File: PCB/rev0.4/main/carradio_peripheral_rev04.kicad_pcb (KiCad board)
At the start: 4 copper layers, 100 x 100 mm, 210 parts, among them J1 ISO 10487 A (via pigtail), J10 Expansion, J12 Display buttons, J13 HDMI in (from VIM3), J14 Display FPC 40P 0.5mm, J18 VIM3 VIN (JST-XH 2P), J2 VIM3 40-pin via 2x20 IDC ribb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, J21 Expansion 2, J22 SWD, J23 Audio module socket, J25 USB module socket, J27 GNSS module socket, J5 VIM3 POWER key lead, J7 BH1750 light sensor, J8 ISO 10487 C1 (via pigtail), Q1 AO3400A, Q10 P-MOSFET -40V, Q11 CSD18543Q3A, Q12 CSD18543Q3A, Q2 P-MOSFET -60V, Q3 2N7002, SW1 BOOTSEL, SW2 RESET, U1 TPS560430XDBVR, U12 TPS55288RPMR, U13 CH334R, U19 AP2112K-3.3, U2 EL817S1(C), U20 RP2350B, U21 W25Q128JVS, U3 EL817S1(C), U4 EL817S1(C), U5 EL817S1(C), U6 LP5907MFX-3.3, Y1 12MHz, Y3 12MHz

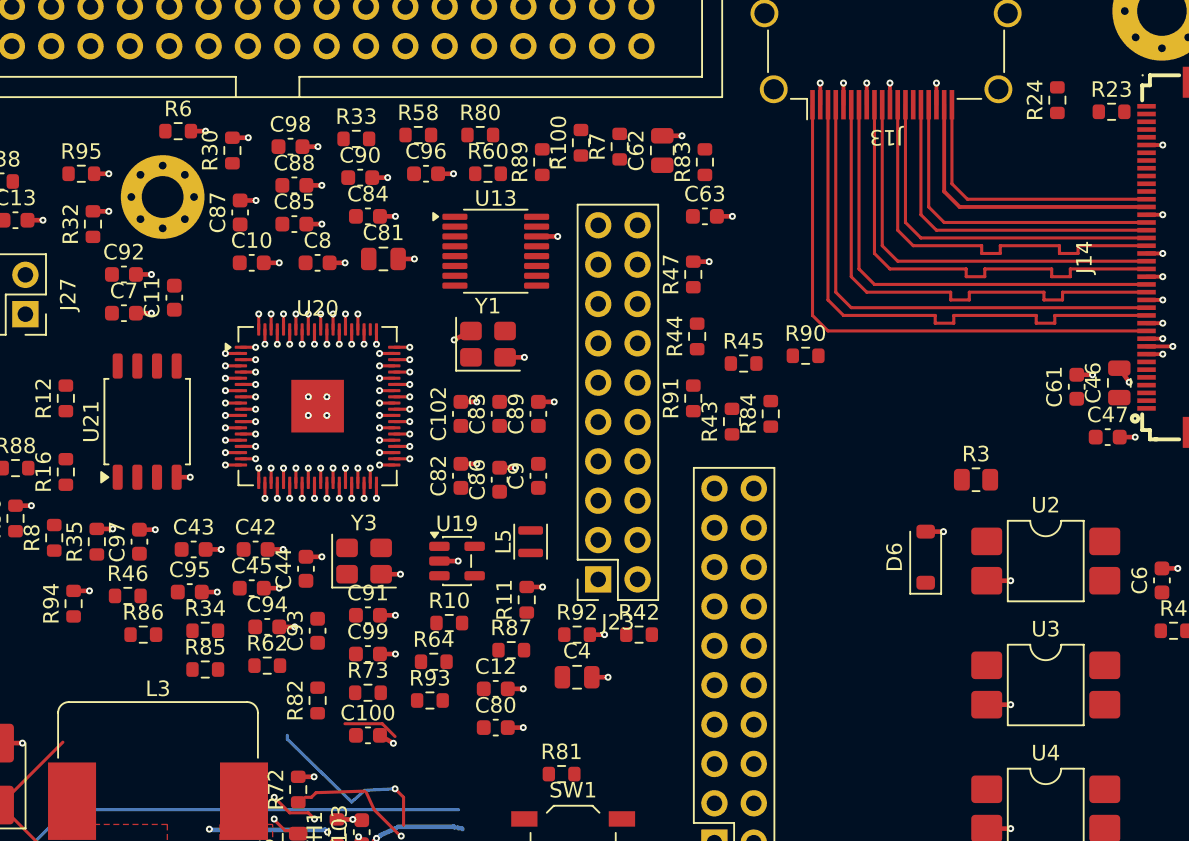
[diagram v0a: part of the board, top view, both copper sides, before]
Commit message: PCB rev 0.4: power hub 1 from the always-on 5V so a blank MCU flashes over USB
Hub 1 (U13) ran from +5V_SYS, which only exists after the MCU firmware
enables the TPS55288, so a blank RP2350B could only be flashed over SWD.
U13 VDD and C61 now sit on +5V_AON, and R104 (10k to HUB_3V3) keeps the
hub out of reset while the blank MCU's pads default to pull-down.
README gains a flashing section.

Co-Authored-By: Claude Opus 5.5 (1M context) <noreply@anthropic.com>
Claude-Session: https://claude.ai/code/session_01C8m2AkFwQrNE2yN9Ymgjwu
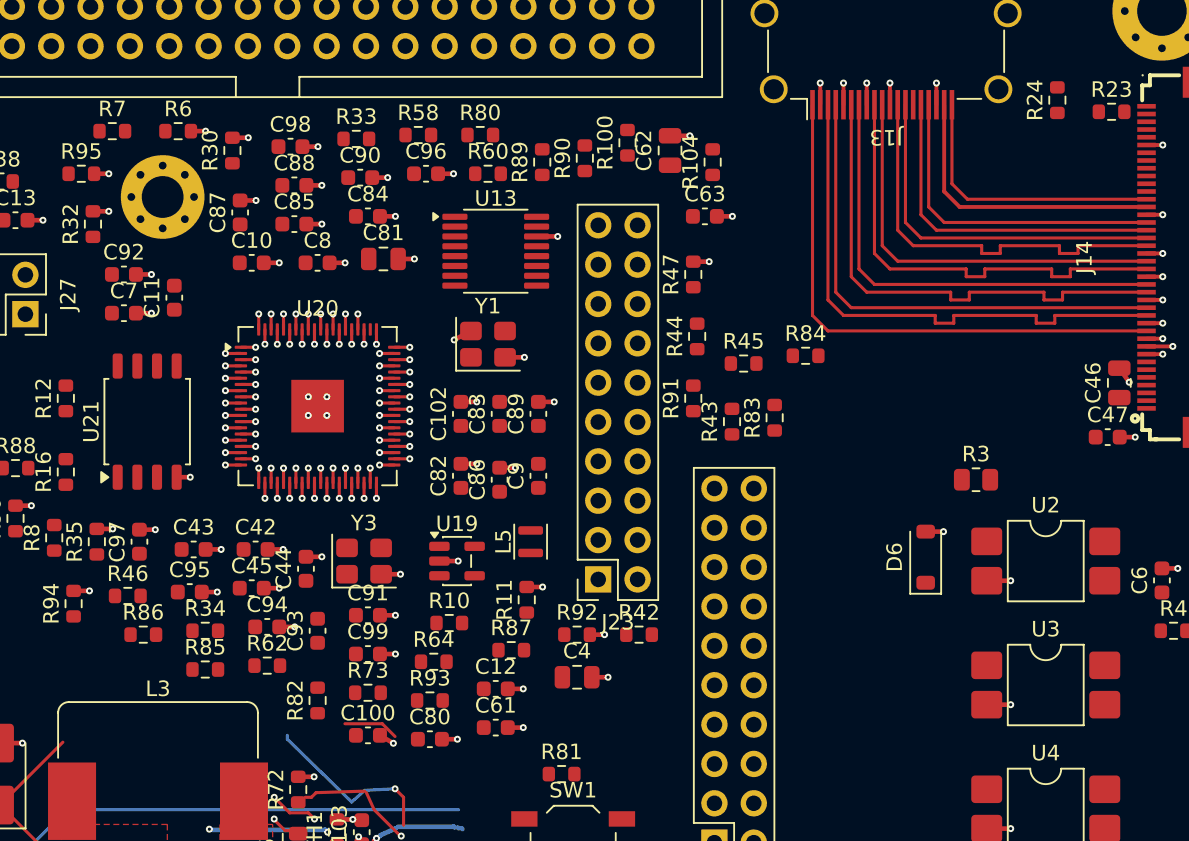
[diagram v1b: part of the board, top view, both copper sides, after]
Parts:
- added R104: 10k, Resistor_SMD:R_0603_1608Metric, F.Cu at (66.5, 14.2)
- moved C61 43.5 mm to (52.5, 50.8), turned to 0 degrees
- moved R7 32.8 mm to (27.8, 12.2), turned to 0 degrees
- moved R90 19.1 mm to (58.2, 14.0), turned to 90 degrees
- moved R83 17.1 mm to (70.5, 30.8)
- moved R84 4.37 mm to (72.5, 26.8), turned to 0 degrees
- moved C80 4.32 mm to (48.2, 51.5)
- moved R100 3.00 mm to (61.0, 13.0)
- moved C62 0.50 mm to (63.8, 13.5)
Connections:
- C61 pad 1: /+5V_SYS -> /+5V_AON
- U13 pad 12: /+5V_SYS -> /+5V_AON

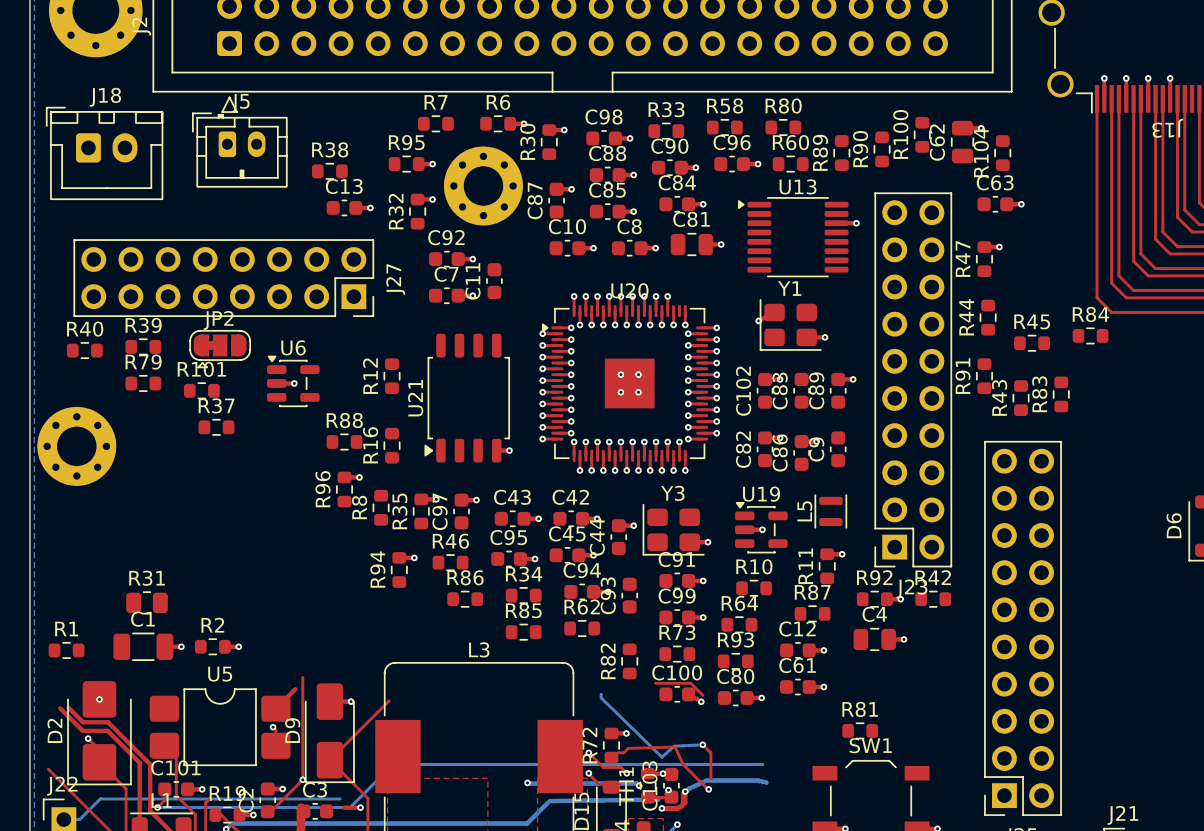
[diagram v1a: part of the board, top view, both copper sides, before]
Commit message: PCB rev 0.4: re-assign RP2350B GPIOs to face their destinations, widen the MCU ring
The autorouter kept failing at the RP2350B because many signals left the
QFN on the side away from their connector. GPIOs are re-assigned
(assign.py: Hungarian assignment on pin-to-destination distance) with
the constraints kept: ADCs on GPIO40-42, GNSS on UART1 GPIO4/5, I2C on
I2C1 GPIO30/31, and a UART pair on J10 pins 2/3 (GPIO32/33) for the
future K-line board. Expansion nets are renamed after their GPIO.

Placement keeps a 2 mm free ring around the QFN (b5.py RING) and
fanmcu.py gives every MCU pin a stub and via before autorouting.
README gains the full GPIO table.

Co-Authored-By: Claude Opus 5.5 (1M context) <noreply@anthropic.com>
Claude-Session: https://claude.ai/code/session_01C8m2AkFwQrNE2yN9Ymgjwu
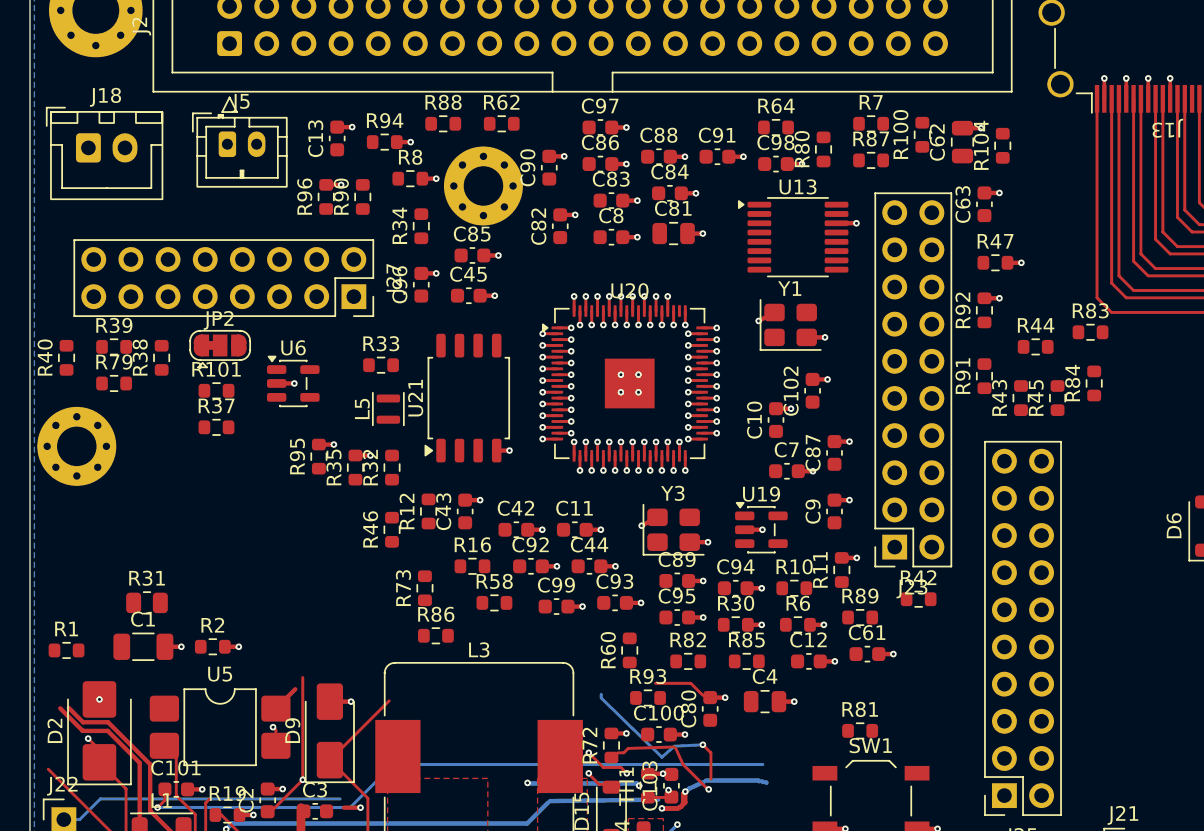
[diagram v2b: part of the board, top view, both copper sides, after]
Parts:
- moved R6 39.9 mm to (52.5, 46.5)
- moved R58 36.1 mm to (31.8, 45.0)
- moved R90 35.6 mm to (22.8, 17.2)
- moved R30 35.4 mm to (48.2, 46.5), turned to 0 degrees
- moved R60 35.0 mm to (41.0, 48.2), turned to 90 degrees
- moved R62 34.9 mm to (32.2, 12.2)
- moved R64 34.1 mm to (51.0, 12.5)
- moved R89 31.8 mm to (56.8, 46.0), turned to 0 degrees
- moved R87 31.3 mm to (57.5, 14.8)
- moved L5 31.0 mm to (24.5, 31.8)
- moved R7 29.8 mm to (57.5, 12.2)
- moved R94 29.3 mm to (24.2, 13.5), turned to 0 degrees
- moved C91 29.1 mm to (47.0, 14.5)
- moved C97 27.9 mm to (39.0, 12.5), turned to 0 degrees
- moved R34 26.2 mm to (26.8, 19.2), turned to 90 degrees
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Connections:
- J10 pad 2: /EXP_GP20 -> /EXP_GP32
- J10 pad 3: /EXP_GP21 -> /EXP_GP33
- J10 pad 4: /EXP_GP30 -> /EXP_GP28
- J10 pad 8: /EXP_GP31 -> /EXP_GP13
- J21 pad 2: /EXP_GP32 -> /EXP_GP34
- J21 pad 3: /EXP_GP33 -> /EXP_GP29
- J21 pad 4: /EXP_GP34 -> /EXP_GP11
- J21 pad 5: /EXP_GP35 -> /EXP_GP12
- J21 pad 6: /EXP_GP36 -> /EXP_GP27
- J21 pad 7: /EXP_GP37 -> /EXP_GP26
- J21 pad 8: /EXP_GP38 -> /EXP_GP25
- J21 pad 9: /EXP_GP39 -> /EXP_GP24
- U20 pad 1: /LUX_SDA -> /MCU_GNSS_TX
- U20 pad 11: /MCU_GNSS_EN -> /EXP_GP12
- U20 pad 12: /MCU_SBC_SENSE -> /EXP_GP13
- U20 pad 13: /MCU_SERVICE -> /MCU_PARK_IN
- U20 pad 14: /MCU_DAC_MUTE -> /MCU_PWR_KEY
- U20 pad 16: /MCU_BTN_SCREEN -> /MCU_BTN_MUTE
- U20 pad 18: /MCU_GNSS_RST -> /MCU_BTN_SCREEN
- U20 pad 19: /MCU_GNSS_PPS -> /MCU_SERVICE
- U20 pad 2: /LUX_SCL -> /MCU_GNSS_RX
- U20 pad 20: /EXP_GP20 -> /MCU_AMP_EN
- U20 pad 21: /EXP_GP21 -> /MCU_LED
- U20 pad 23: /MCU_USBP_FAULT1 -> /MCU_VIM3_PWR_EN
- U20 pad 25: /MCU_USBP_FAULT2 -> /EXP_GP24
- U20 pad 26: /MCU_LED -> /EXP_GP25
- U20 pad 27: /MCU_USBP_PG -> /EXP_GP26
- U20 pad 28: /MCU_BTN_MUTE -> /EXP_GP27
- U20 pad 3: /MCU_ILLUM_IN -> /MCU_SBC_SENSE
- U20 pad 36: /MCU_VIM3_PWR_EN -> /EXP_GP28
- U20 pad 37: /MCU_GNSS_SAFEBOOT -> /EXP_GP29
- U20 pad 38: /EXP_GP30 -> /LUX_SDA
- U20 pad 39: /EXP_GP31 -> /LUX_SCL
- U20 pad 4: /MCU_PARK_IN -> /MCU_GNSS_RST
- U20 pad 44: /EXP_GP35 -> /MCU_REV_IN
- U20 pad 45: /EXP_GP36 -> /MCU_USBP_PG
- U20 pad 46: /EXP_GP37 -> /MCU_ILLUM_IN
- U20 pad 47: /EXP_GP38 -> /MCU_USBP_FAULT2
- U20 pad 48: /EXP_GP39 -> /MCU_USBP_FAULT1
- U20 pad 54: /MCU_HUB_RST -> /MCU_ACC_IN
- U20 pad 6: /MCU_PWR_KEY -> /MCU_GNSS_SAFEBOOT
- U20 pad 7: /MCU_AMP_EN -> /MCU_GNSS_EN
- U20 pad 77: /MCU_GNSS_TX -> /MCU_BL_EN
- U20 pad 78: /MCU_GNSS_RX -> /MCU_BL_PWM
- U20 pad 79: /MCU_ACC_IN -> /MCU_HUB_RST
- U20 pad 8: /MCU_BL_EN -> /MCU_DAC_MUTE
- U20 pad 80: /MCU_REV_IN -> /MCU_GNSS_PPS
- U20 pad 9: /MCU_BL_PWM -> /EXP_GP11
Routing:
- net GND: track 124.9 -> 130.1 mm, vias 120 -> 125
- net /EXP_GP39: track 1.00 -> 0.00 mm, vias 1 -> 0
- net /EXP_GP37: track 1.00 -> 0.00 mm, vias 1 -> 0
- net /EXP_GP35: track 1.00 -> 0.00 mm, vias 1 -> 0
- net /EXP_GP30: track 1.00 -> 0.00 mm, vias 1 -> 0
- net /EXP_GP28: track 0.00 -> 1.00 mm, vias 0 -> 1
- net /EXP_GP27: track 0.00 -> 1.00 mm, vias 0 -> 1
- net /EXP_GP25: track 0.00 -> 1.00 mm, vias 0 -> 1
- net /EXP_GP20: track 1.00 -> 0.00 mm, vias 1 -> 0
- net /EXP_GP13: track 0.00 -> 1.00 mm, vias 0 -> 1
- net /EXP_GP38: track 0.95 -> 0.00 mm, vias 1 -> 0
- net /EXP_GP36: track 0.95 -> 0.00 mm, vias 1 -> 0
- net /EXP_GP31: track 0.95 -> 0.00 mm, vias 1 -> 0
- net /EXP_GP29: track 0.00 -> 0.95 mm, vias 0 -> 1
- net /EXP_GP26: track 0.00 -> 0.95 mm, vias 0 -> 1
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
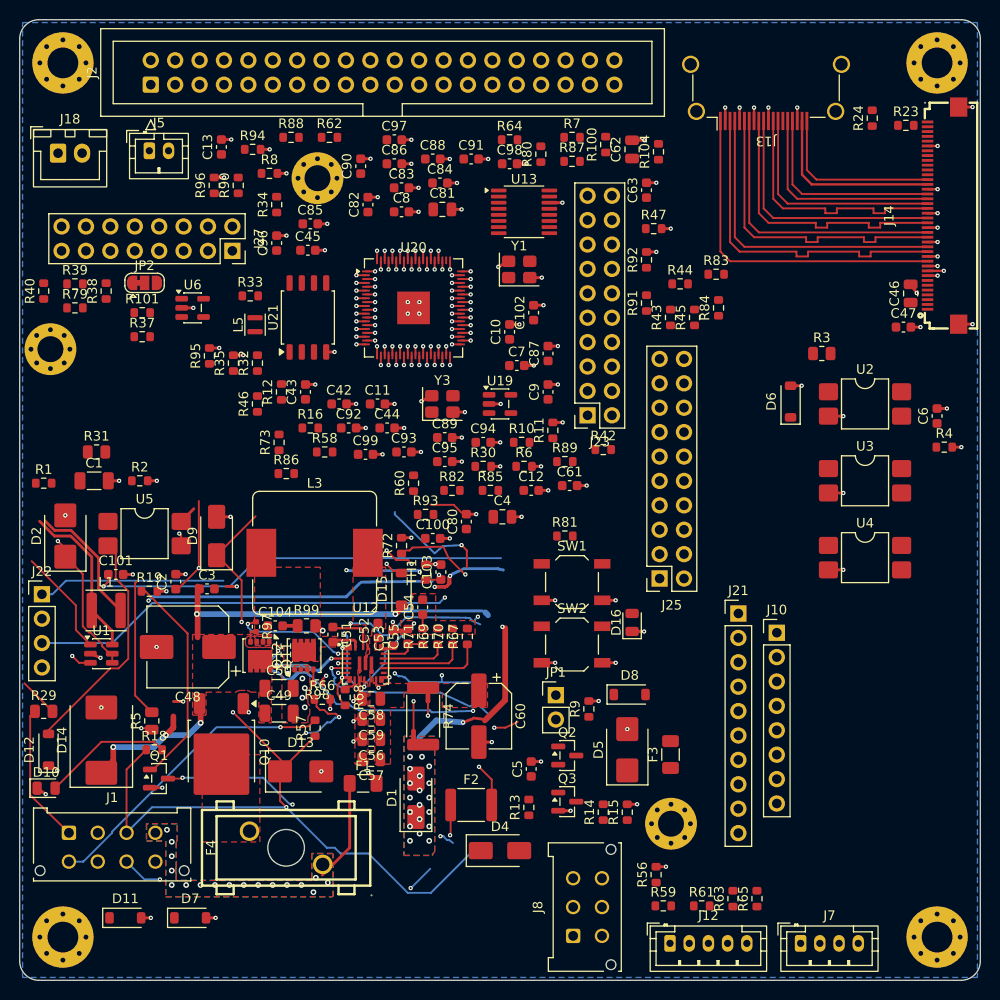
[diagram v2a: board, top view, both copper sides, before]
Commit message: PCB rev 0.4: main board fully routed (DRC 0 unconnected, no errors)
Freerouting (five parallel runs) plus maze2b got the board from 292 to 18
unconnected; the rest was finished with a new single-connection grid
router (bridge.py) with optional rip-up.

Fixes on the way:
- VSYS_IN feed track ran past its via into C3 pad 1 (BUCK_CB); cut back.
- The RP2350B inner escape vias (0.8 mm pitch, 0.35 mm gaps) walled in the
  exposed pad GND and the pins escaping inward. The unused pin 61 inner
  via is gone and every other inner via sits 0.8 mm further in (10 of 19),
  opening 1.15 mm gaps; the EP GND now reaches the planes.
- In1 ILLUM_LED moved clear of the J1 peg hole (BATT_RAW stitching vias
  shifted 0.1 mm), J23/J25 socket GND pins connect solid (starved thermals).

Review: USB_UP_DP runs single-ended at 0.16 mm, +5V_AON and parts of
+3V3_MCU at 0.2 mm. Scripts adapted for native KiCad 10 on Windows;
layout/README.md documents the flow.

Co-Authored-By: Claude Opus 5.5 (1M context) <noreply@anthropic.com>
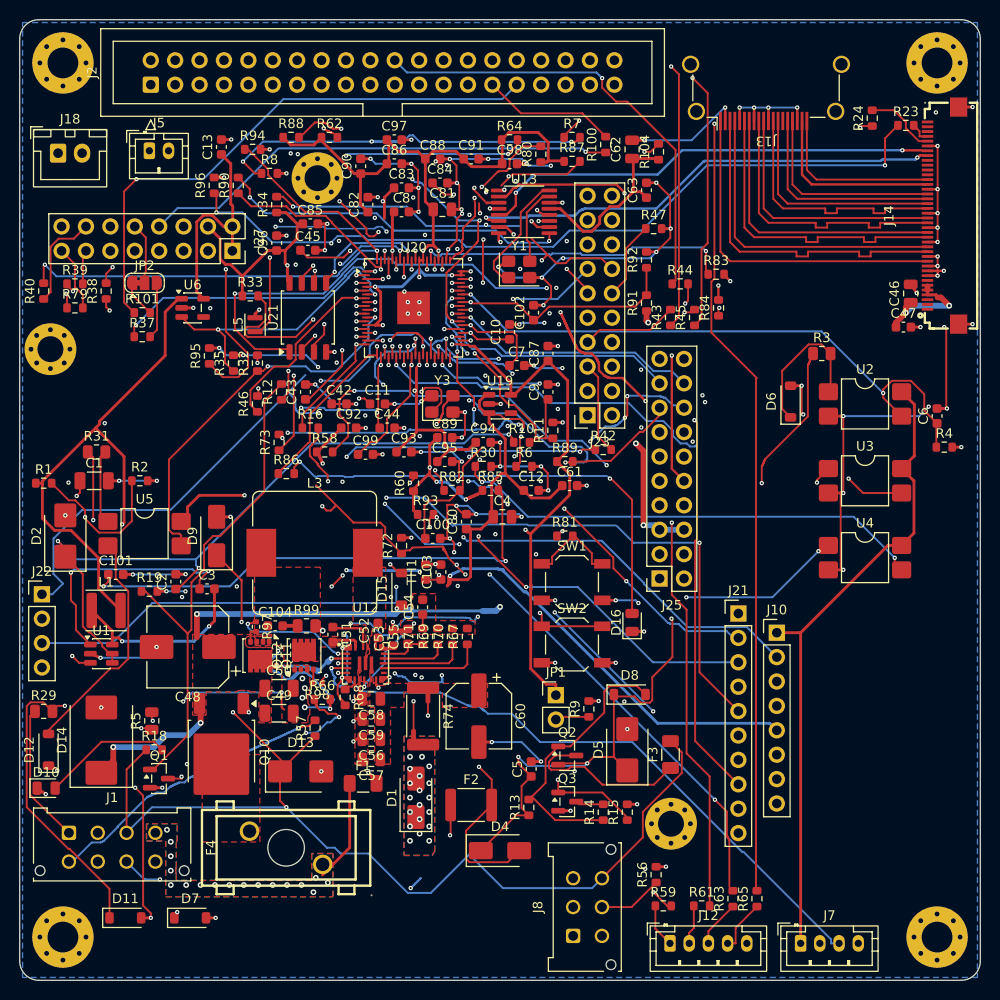
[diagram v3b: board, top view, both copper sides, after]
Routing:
- net GND: track 130.1 -> 727.9 mm, vias 125 -> 154
- net /+3V3_MCU: track 13.6 -> 354.9 mm, vias 12 -> 19
- net /+5V_AON: track 33.5 -> 200.4 mm, vias 4 -> 8
- net /ACC_P: track 0.00 -> 151.2 mm, vias 0 -> 6
- net /LUX_SDA: track 41.5 -> 191.1 mm, vias 6 -> 9
- net /MCU_BTN_MUTE: track 1.00 -> 148.3 mm, vias 1 -> 5
- net /LUX_SCL: track 39.9 -> 167.3 mm, vias 3 -> 7
- net /MCU_BTN_VOLDN: track 1.00 -> 115.0 mm, vias 1 -> 10
- net /+5V_SYS: track 17.7 -> 130.1 mm, vias 13 -> 18
- net /REV_LED: track 4.13 -> 115.0 mm, vias 0 -> 3
- net /MCU_BTN_VOLUP: track 0.95 -> 105.6 mm, vias 1 -> 5
- net /VBAT_P: track 26.1 -> 127.2 mm, vias 6 -> 9
- net /MCU_BTN_SCREEN: track 1.00 -> 94.7 mm, vias 1 -> 4
- net /MCU_BL_EN: track 0.95 -> 91.7 mm, vias 1 -> 4
- net /ILLUM_LED: track 14.5 -> 103.0 mm, vias 0 -> 3
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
